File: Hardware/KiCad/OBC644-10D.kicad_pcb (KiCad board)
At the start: 2 copper layers, 45 x 45 mm, 62 parts, among them J1 CONN_11, J2 CONN_11, J3 CONN_4, J4 CONN_6, J5 CONN_2, U1 LT1761ES5-3.3, U10 LT1761ES5-xx, U11 LT1761ES5-xx, U12 M25P80, U2 ATMEGA644PA-A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

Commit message: fix spacing
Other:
- rule trace_min: 0.127 -> 0.15

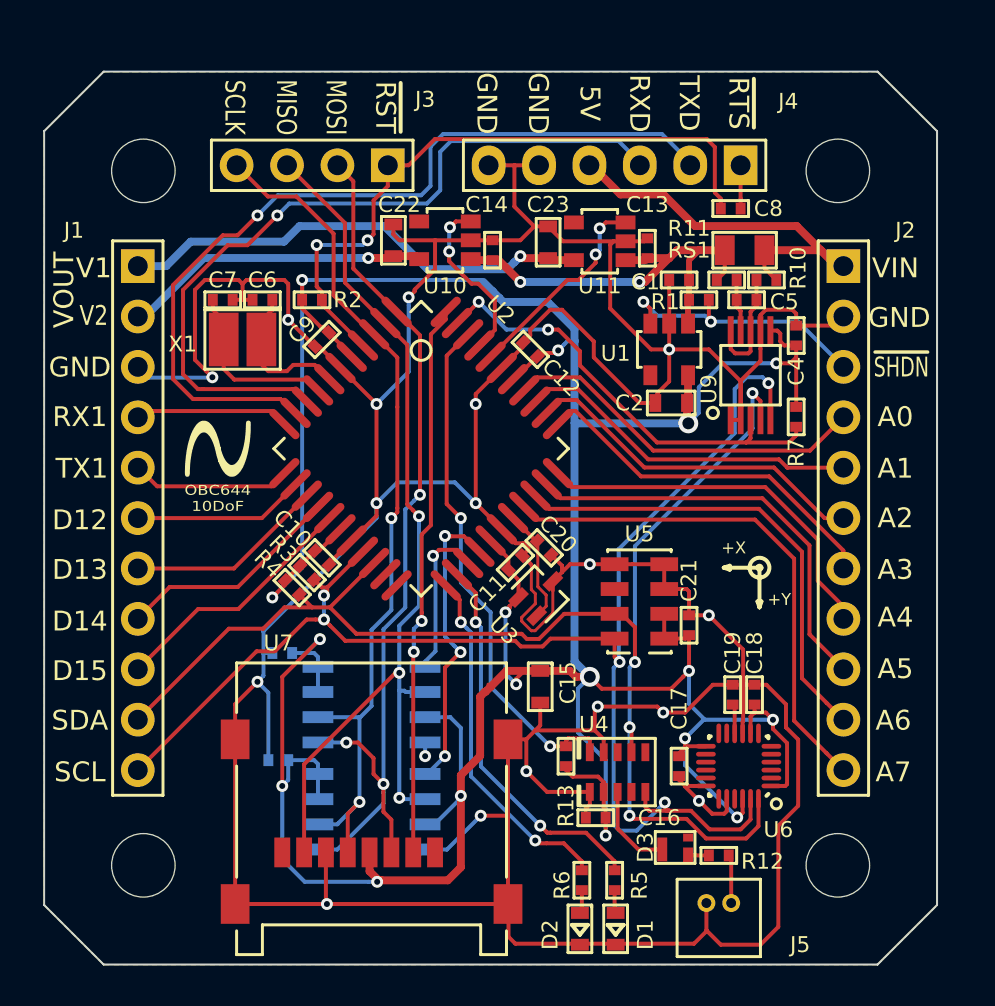
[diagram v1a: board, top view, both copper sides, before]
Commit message: Fix PCB and schematic
fix ShuntResistor size & routing
change R5,R6 value
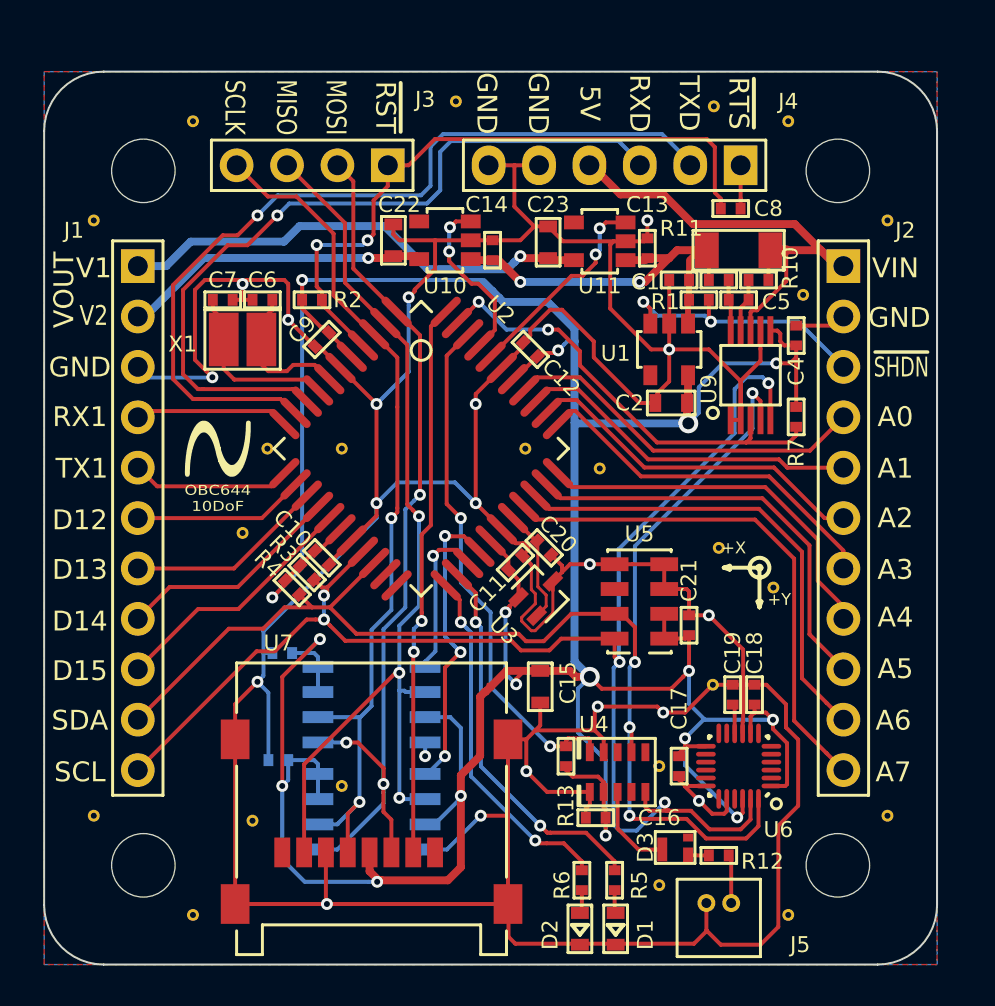
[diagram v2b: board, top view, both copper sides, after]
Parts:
- added REF**: VIA_03, DRILL_HOLE:VIA_03, F.Cu at (130.0, 85.0)
- added REF**: VIA_03, DRILL_HOLE:VIA_03, F.Cu at (142.5, 96.5)
- added REF**: VIA_03, DRILL_HOLE:VIA_03, F.Cu at (164.2, 103.5)
- added REF**: VIA_03, DRILL_HOLE:VIA_03, F.Cu at (165.8, 88.8)
- added REF**: VIA_03, DRILL_HOLE:VIA_03, F.Cu at (161.2, 79.2)
- added REF**: VIA_03, DRILL_HOLE:VIA_03, F.Cu at (148.2, 79.0)
- added REF**: VIA_03, DRILL_HOLE:VIA_03, F.Cu at (138.8, 96.5)
- added REF**: VIA_03, DRILL_HOLE:VIA_03, F.Cu at (137.5, 100.8)
- added REF**: VIA_03, DRILL_HOLE:VIA_03, F.Cu at (138.0, 115.2)
- added REF**: VIA_03, DRILL_HOLE:VIA_03, F.Cu at (142.5, 113.5)
- added REF**: VIA_03, DRILL_HOLE:VIA_03, F.Cu at (158.5, 118.5)
- added REF**: VIA_03, DRILL_HOLE:VIA_03, F.Cu at (135.0, 80.0)
- added REF**: VIA_03, DRILL_HOLE:VIA_03, F.Cu at (158.5, 112.5)
- added REF**: VIA_03, DRILL_HOLE:VIA_03, F.Cu at (161.2, 108.4)
- added REF**: VIA_03, DRILL_HOLE:VIA_03, F.Cu at (161.5, 101.5)
- added REF**: VIA_03, DRILL_HOLE:VIA_03, F.Cu at (155.5, 97.5)
- added REF**: VIA_03, DRILL_HOLE:VIA_03, F.Cu at (165.0, 80.0)
- added REF**: VIA_03, DRILL_HOLE:VIA_03, F.Cu at (170.0, 85.0)
- added REF**: VIA_03, DRILL_HOLE:VIA_03, F.Cu at (170.0, 115.0)
- added REF**: VIA_03, DRILL_HOLE:VIA_03, F.Cu at (165.0, 120.0)
- added REF**: VIA_03, DRILL_HOLE:VIA_03, F.Cu at (130.0, 115.0)
- added REF**: VIA_03, DRILL_HOLE:VIA_03, F.Cu at (135.0, 120.0)
- added REF**: VIA_03, DRILL_HOLE:VIA_03, F.Cu at (151.8, 96.5)
- D1, D2: value LED -> SML-D12M8WT86
- J5: value CONN_2 -> 53047
- RS1: footprint EIA:0805 -> EIA:1206
- U12: value M25P80 -> M25XX_ROM2
- U2: value ATMEGA644PA-A -> ATMEGA644PA-AUR
- U3: value REF3320 -> REF3320AIDCKT
- U5: value MS5611 -> MS561101BA03-00
- U7: value microSD_hinge -> microSD_hinge 0472192001
- U8: value M25P80 -> M25XX_ROM1
- U9: value INA226 -> INA226AQDGSRQ1
- X1: value CRYSTAL -> NX3225GD-8MHZ
- moved C5 0.40 mm to (162.5, 89.0)
- moved R10 0.40 mm to (163.5, 88.0)
- moved R11 0.40 mm to (161.5, 88.0)
- moved RS1 0.30 mm to (162.5, 86.5)
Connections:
- U9 pad 10: Net-(C5-Pad2) -> Net-(C5-Pad1)
- U9 pad 8: Net-(C5-Pad2) -> /VIN
- U9 pad 9: Net-(C5-Pad1) -> Net-(C5-Pad2)
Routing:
- net /VIN: track 21.1 -> 25.5 mm
- net Net-(C5-Pad2): track 5.78 -> 2.72 mm
- net GND: track 267.5 -> 265.1 mm, vias 18 -> 20
- net /VDD1: track 21.8 -> 20.4 mm

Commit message: Add VCPU OUTPUT
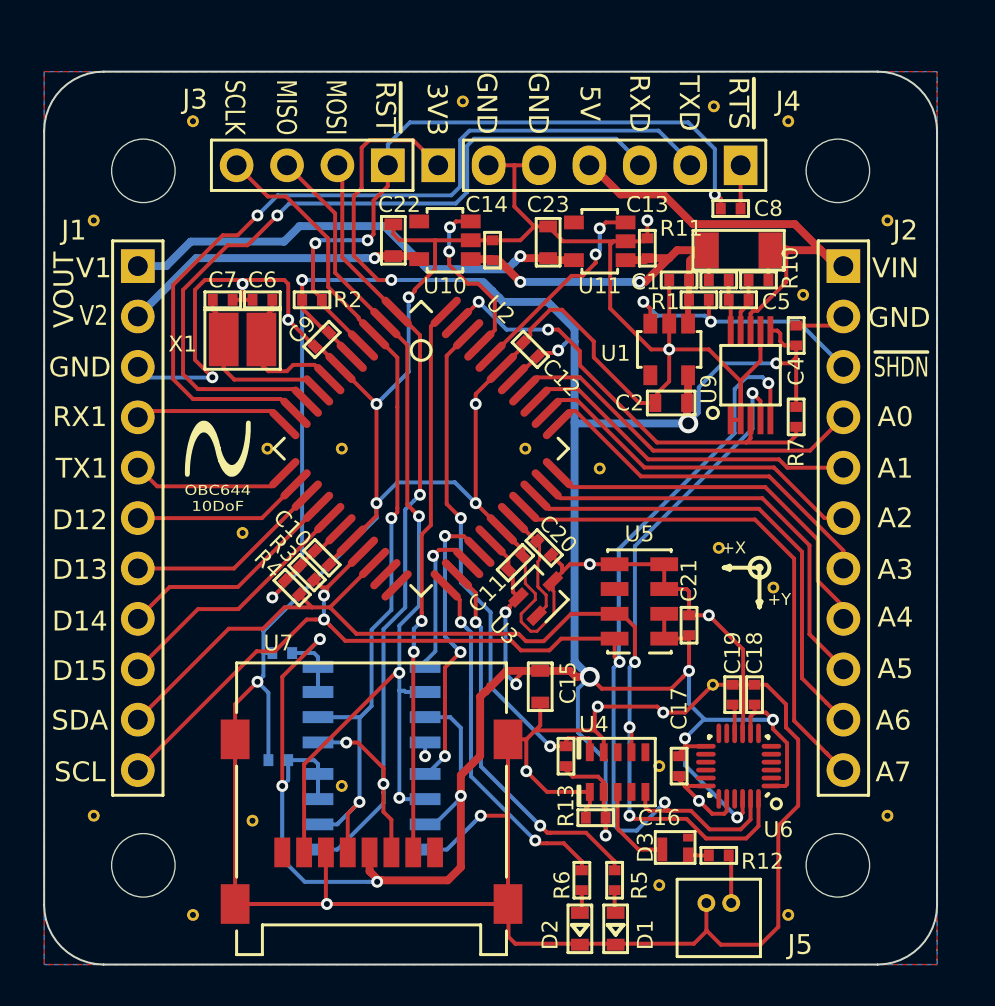
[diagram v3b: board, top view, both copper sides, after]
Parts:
- added J6: CONN_1, CONN_2.54MM:1P, F.Cu at (147.3, 82.1)
- R5, R6: value 3.3k -> 1k
- moved REF** 0.35 mm to (148.6, 79.0)
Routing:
- net +3.3V: track 196.9 -> 209.5 mm, vias 17 -> 18
- net /~RST: track 33.3 -> 34.9 mm, vias 2 -> 3
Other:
- net class PWR removed
- board text added: "3V3"

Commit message: Update Rev:E
Add some Pins (3V3, UART_GPIO)
Change SO8-ROM Footprints
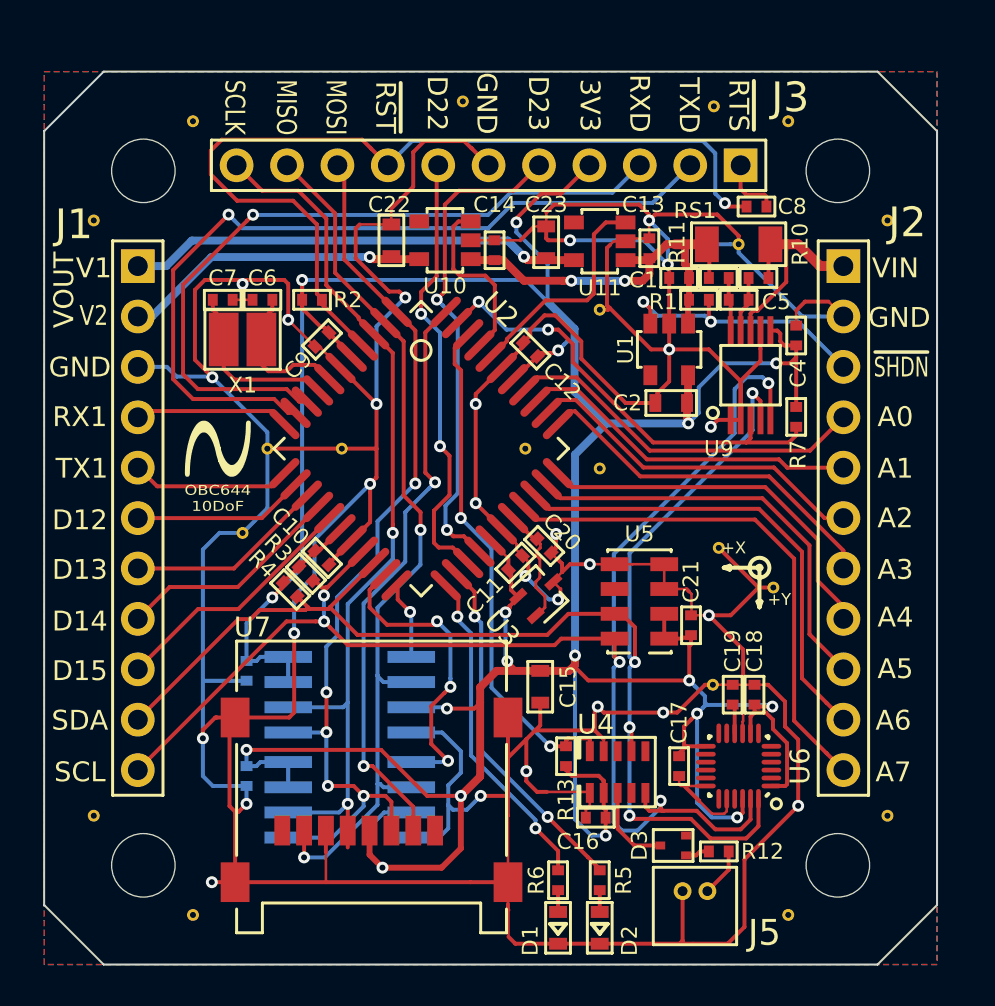
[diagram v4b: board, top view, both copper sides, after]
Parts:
- removed J4: CONN_6, CONN_2.54MM:1x6DP
- removed J6: CONN_1, CONN_2.54MM:1P
- removed the REF** at (165.8, 88.8)
- removed the REF** at (138.0, 115.2)
- removed the REF** at (142.5, 113.5)
- removed the REF** at (158.5, 118.5)
- removed the REF** at (158.5, 112.5)
- added G***: LOGO, LOGO:N_LOGO_3mm, B.Cu at (151.5, 93.0)
- added REF**: VIA_03, DRILL_HOLE:VIA_03, F.Cu at (162.5, 86.2)
- added REF**: VIA_03, DRILL_HOLE:VIA_03, F.Cu at (155.5, 89.5)
- D1, D2: footprint DIODE:0603 -> DIODE:D_0603
- D3: footprint DIODE:SOT523HY -> DIODE:SOT-523
- J3: value CONN_4 -> CONN_11; footprint CONN_2.54MM:1x4P -> CONN_2.54MM:1x11P
- U1, U10, U11: footprint TI:SOT-25 -> IC:SOT25
- U12, U8: footprint TI:SO8 -> IC:SO8NW
- U2: footprint QFP_QFN:TQFP_44 -> IC:QFP44
- U3: footprint TI:SC-70 -> IC:SC70_3
- U6: footprint QFP_QFN:QFN24 -> IC:QFN24
- U9: footprint TI:MSOP10 -> IC:MSOP10
- moved J3 8.89 mm to (149.9, 82.2)
- moved D1 2.90 mm to (153.4, 120.7)
- moved C24 2.01 mm to (137.7, 107.7), turned to 270 degrees
- moved C3 1.79 mm to (137.7, 113.0), turned to 270 degrees
- moved J5 1.34 mm to (160.3, 118.8)
- moved C8 1.30 mm to (163.4, 84.3)
- moved U8 1.25 mm to (142.9, 114.2)
- moved U12 1.21 mm to (142.9, 108.9)
- moved R6 1.20 mm to (153.4, 118.2)
- moved U7 1.10 mm to (144.0, 115.0)
- moved D2 1.00 mm to (155.5, 120.7)
- moved R5 0.75 mm to (155.5, 118.2)
- moved RS1 0.30 mm to (162.5, 86.2)
- moved R12 0.20 mm to (161.5, 116.8)
- moved D3 0.14 mm to (159.2, 116.5)
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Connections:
- net /INT1 renamed /D2
- net /INT2 renamed /D3
- net /~SS1 renamed /D4
- D3 pad 2: (no net) -> Net-(D3-Pad2)
- J3 pad 1: /~RST -> /~PROG
- J3 pad 2: /MOSI -> /TX0
- J3 pad 3: /MISO -> /RX0
- J3 pad 4: /SCLK -> +3.3V
- R5 pad 2: Net-(D1-Pad1) -> Net-(D2-Pad1)
- R6 pad 2: Net-(D2-Pad1) -> Net-(D1-Pad1)
- U1 pad 4: (no net) -> Net-(U1-Pad4)
- U10 pad 4: (no net) -> Net-(U10-Pad4)
- U11 pad 4: (no net) -> Net-(U11-Pad4)
- U12 pad 1: /~SS3 -> /D19
- U2 pad 21: (no net) -> /D18
- U2 pad 22: (no net) -> /D19
- U2 pad 25: /~SS3 -> /D22
- U2 pad 26: /~SS2 -> /D23
- U4 pad 4: (no net) -> Net-(U4-Pad4)
- U4 pad 6: (no net) -> Net-(U4-Pad6)
- U4 pad 8: (no net) -> Net-(U4-Pad8)
- U5 pad 6: (no net) -> Net-(U5-Pad6)
- U6 pad 11: (no net) -> Net-(U6-Pad11)
- U6 pad 12: (no net) -> Net-(U6-Pad12)
- U6 pad 14: (no net) -> Net-(U6-Pad14)
- U6 pad 15: (no net) -> Net-(U6-Pad15)
- U6 pad 16: (no net) -> Net-(U6-Pad16)
- U6 pad 17: (no net) -> Net-(U6-Pad17)
- U6 pad 19: (no net) -> Net-(U6-Pad19)
- U6 pad 2: (no net) -> Net-(U6-Pad2)
- U6 pad 21: (no net) -> Net-(U6-Pad21)
- U6 pad 3: (no net) -> Net-(U6-Pad3)
- U6 pad 4: (no net) -> Net-(U6-Pad4)
- U6 pad 5: (no net) -> Net-(U6-Pad5)
- U6 pad 6: (no net) -> Net-(U6-Pad6)
- U6 pad 7: (no net) -> Net-(U6-Pad7)
- U7 pad 1: (no net) -> Net-(U7-Pad1)
- U7 pad 8: (no net) -> Net-(U7-Pad8)
- U8 pad 1: /~SS2 -> /D18
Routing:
- net GND: track 264.8 -> 342.2 mm, vias 20 -> 27
- net /D23: track 0.00 -> 24.9 mm, vias 0 -> 2
- net /D22: track 0.00 -> 23.4 mm, vias 0 -> 2
- net /D18: track 0.00 -> 16.8 mm, vias 0 -> 3
- net /~SS2: track 15.3 -> 0.00 mm, vias 3 -> 0
- net /VIN: track 25.5 -> 11.7 mm
- net /~RST: track 34.9 -> 45.5 mm, vias 3 -> 1
- net /~SS3: track 8.05 -> 0.00 mm, vias 1 -> 0
- net +3.3V: track 209.5 -> 205.4 mm
- net /D19: track 0.00 -> 3.91 mm, vias 0 -> 1
- net /D4: track 28.1 -> 31.1 mm
- net /MISO: track 48.8 -> 46.0 mm, vias 3 -> 2
- net /RX0: track 39.2 -> 37.0 mm
- net /TX0: track 43.1 -> 41.3 mm
- net /SCLK: track 44.2 -> 45.9 mm
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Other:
- rule pad_to_mask_clearance: 0 -> 0.1
- rule trace_min: 0.15 -> 0.13
- board text added: "644PA 8MHz 1284P 8MHz"
- board text added: "D22"
- board text added: "D23"
- board text added: "Extreame Environment Computing"
- board text added: "OBC644-10D"
- board text added: "PWM"
- board text added: "ROM1 (D18)"
- board text added: "ROM2 (D19)"
- board text added: "Rev:E"
- board text added: "VOUT(D0)"
- board text added: "VOUT(D1)"
- board text added: "_____________"
- board text removed: "5V"
